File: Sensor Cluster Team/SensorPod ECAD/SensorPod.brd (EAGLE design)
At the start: 160 x 100 mm, 40 parts, among them J1 BMP388, J2 BMP388, J3 BMP388, J4 BMP388, J5 BMP388, J6 BMP388

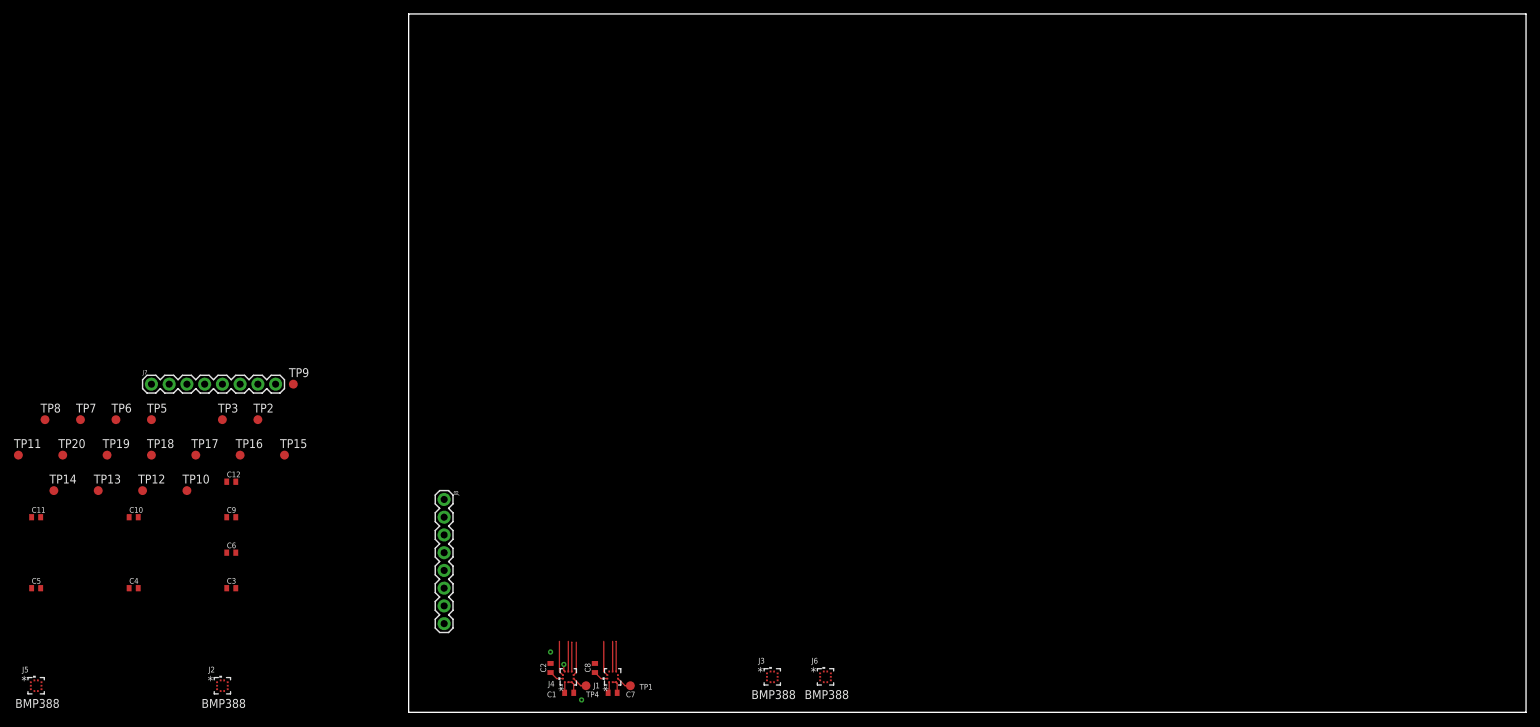
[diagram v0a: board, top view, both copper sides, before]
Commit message: v0_0_1 Sensor Pod Finished
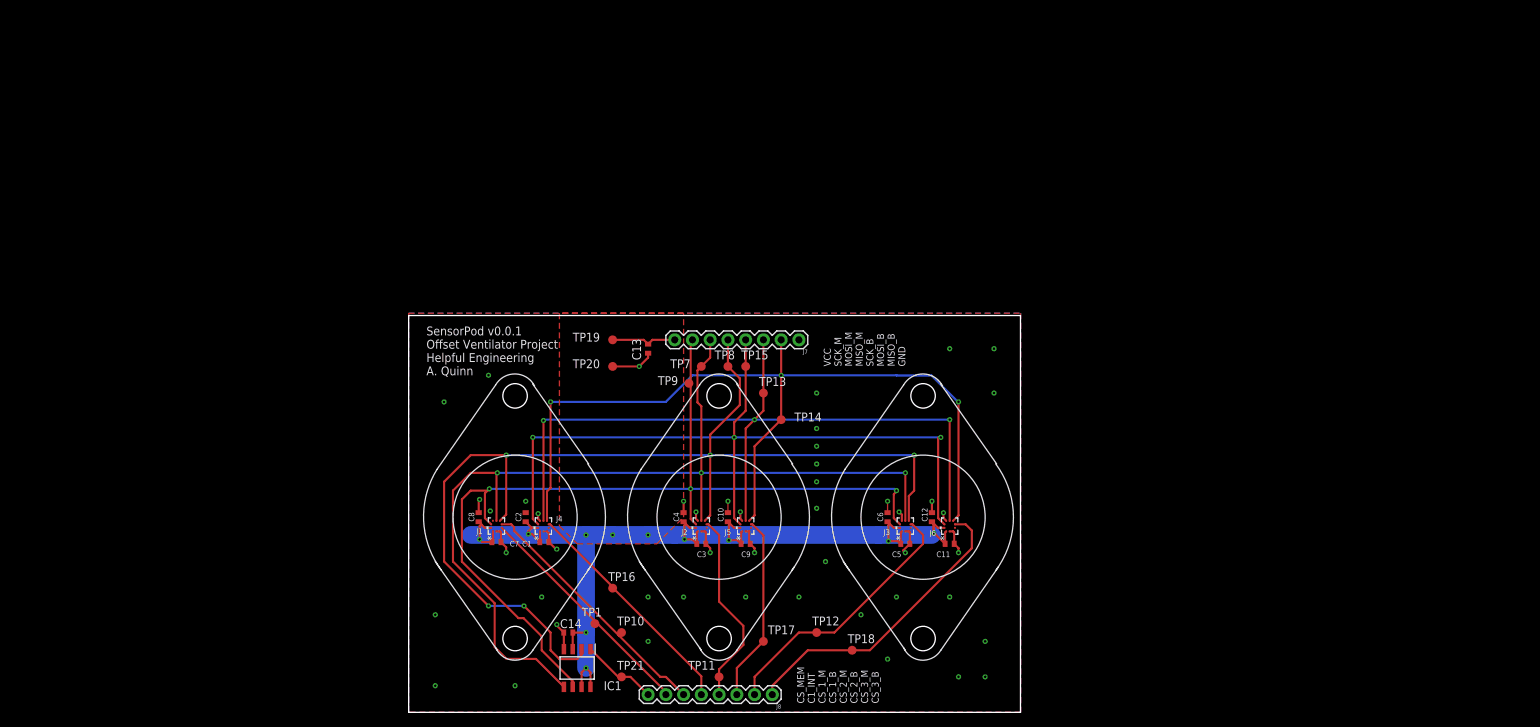
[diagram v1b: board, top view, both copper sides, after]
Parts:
- removed TP2, TP3, TP4, TP5, TP6: TPB1,27, testpad:B1,27
- added C13: 587-3766-1-ND, rcl:C0402
- added C14: 490-7998-1-ND, rcl:C0402
- added IC1: SST25PF040CT-40E_SN, SamacSys_Parts:SOIC127P600X175-8N
- added TP21: TPB1,27, testpad:B1,27
- moved C11 130.9 mm to (77.5, 24.1)
- moved C5 124.6 mm to (71.1, 24.1)
- moved TP11 105.2 mm to (44.5, 5.08)
- moved TP14 104.6 mm to (53.3, 41.9)
- moved TP18 104.1 mm to (63.5, 8.89)
- moved J5 104.1 mm to (48.3, 26.7), turned to 90 degrees
- moved C12 100.5 mm to (74.9, 27.9), turned to 90 degrees
- moved TP12 98.6 mm to (58.4, 11.4)
- moved TP8 98.1 mm to (45.7, 49.5)
- moved TP13 96.3 mm to (50.8, 45.7)
- moved C6 94.1 mm to (68.6, 27.9), turned to 90 degrees
- moved J7 92.9 mm to (55.9, 53.3), turned to 180 degrees
- moved TP7 89.2 mm to (41.9, 49.5)
- moved TP17 85.5 mm to (50.8, 10.2)
- moved C10 85.1 mm to (45.7, 27.9), turned to 90 degrees
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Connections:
- removed net N$1: J1.7, TP1.TP
- removed net N$2: J2.7, TP2.TP
- removed net N$3: J3.7, TP3.TP
- removed net N$4: J4.7, TP4.TP
- removed net N$5: J5.7, TP5.TP
- removed net N$6: J6.7, TP6.TP
- new net C1_INT: J1.7, J8.7, TP1.TP
- new net CS_MEM: IC1.1, J8.8, TP21.TP
- net CS_1_BAK: now also J8.5; no longer J8.4
- net CS_1_MAIN: now also J8.6; no longer J7.4
- net CS_2_MAIN: now also J8.4; no longer J7.3
- net CS_3_BAK: now also J8.1; no longer J8.2
- net CS_3_MAIN: now also J8.2; no longer J7.2
- net GND: now also C13.2, C14.2, IC1.4; no longer J8.1
- net MISO_BAK: now also J7.2; no longer J8.6
- net MISO_MAIN: now also IC1.2, J7.5; no longer J7.6
- net MOSI_BAK: now also J7.3; no longer J8.7
- net MOSI_MAIN: now also IC1.5, J7.6; no longer J7.7
- net SCK_BAK: now also J7.4; no longer J8.5
- net SCK_MAIN: now also IC1.6, J7.7; no longer J7.5
- net VCC: now also C13.1, C14.1, IC1.3, IC1.7, IC1.8; no longer J8.8
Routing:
- net VCC: track 7.40 -> 160.8 mm, vias 0 -> 11
- net MISO_MAIN: track 4.32 -> 156.5 mm, vias 0 -> 5
- net MOSI_MAIN: track 4.32 -> 143.6 mm, vias 0 -> 3
- net SCK_MAIN: track 5.04 -> 135.0 mm, vias 0 -> 3
- net MISO_BAK: track 4.19 -> 124.0 mm, vias 0 -> 3
- net MOSI_BAK: track 4.32 -> 114.0 mm, vias 0 -> 3
- net SCK_BAK: track 5.04 -> 111.8 mm, vias 0 -> 3
- net GND: track 5.30 -> 48.6 mm, vias 1 -> 48
- net CS_3_BAK: track 0.00 -> 43.3 mm
- net CS_3_MAIN: track 0.00 -> 38.2 mm
- net CS_1_MAIN: track 0.00 -> 37.0 mm
- net C1_INT: track 0.00 -> 33.9 mm
- net CS_1_BAK: track 4.86 -> 33.6 mm
- net CS_2_MAIN: track 0.00 -> 28.2 mm
- net CS_2_BAK: track 0.00 -> 26.8 mm
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- added copper zone on layer 1, net GND
- added copper zone on layer 16, net GND
- added copper zone on layer 1, net VCC
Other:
- board size 160 x 100 mm -> 87.6 x 56.8 mm
- board text added: "CS_MEM C1_INT CS_1_M CS_1_B CS_2_M CS_2_B CS_3_M CS_3_B"
- board text added: "SensorPod v0.0.1 Offset Ventilator Project Helpful Engineering A. Quinn"
- board text added: "VCC SCK_M MOSI_M MISO_M SCK_B MOSI_B MISO_B GND"
